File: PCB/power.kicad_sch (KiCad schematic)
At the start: 21 parts, among them U5 TLV62569DBVR, U6 TLV62569DBVR, U7 TLV62569DBVR

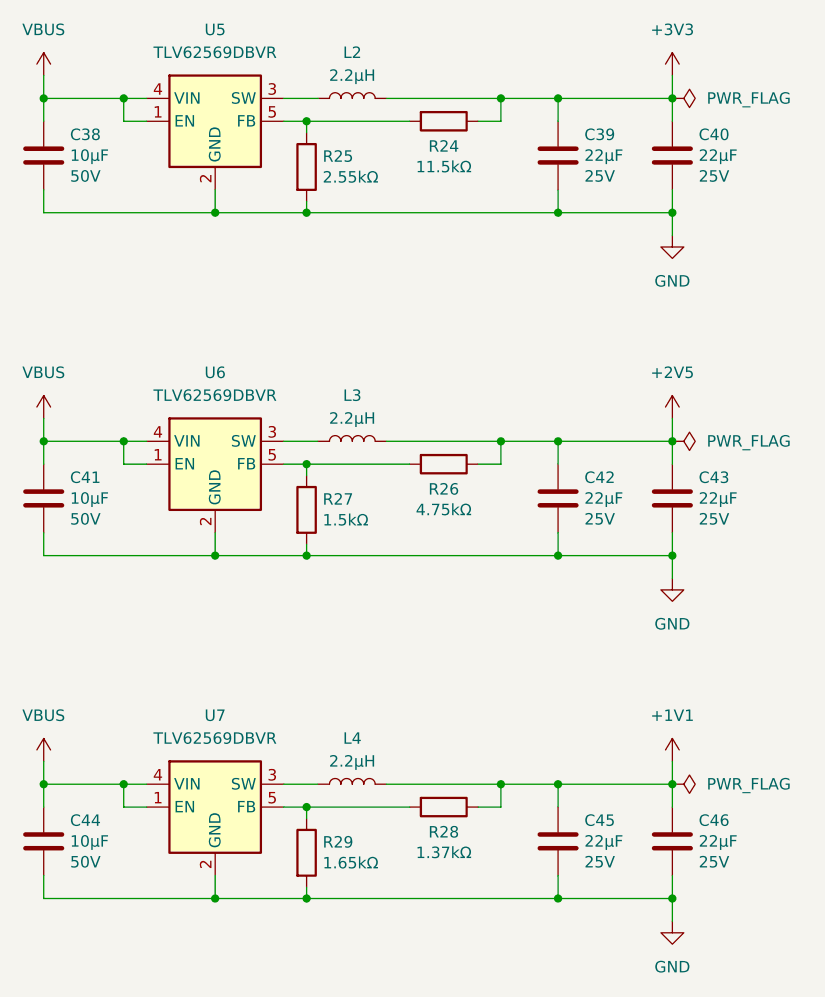
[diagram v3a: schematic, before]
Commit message: Improve the CH347F schematics and added 3D models
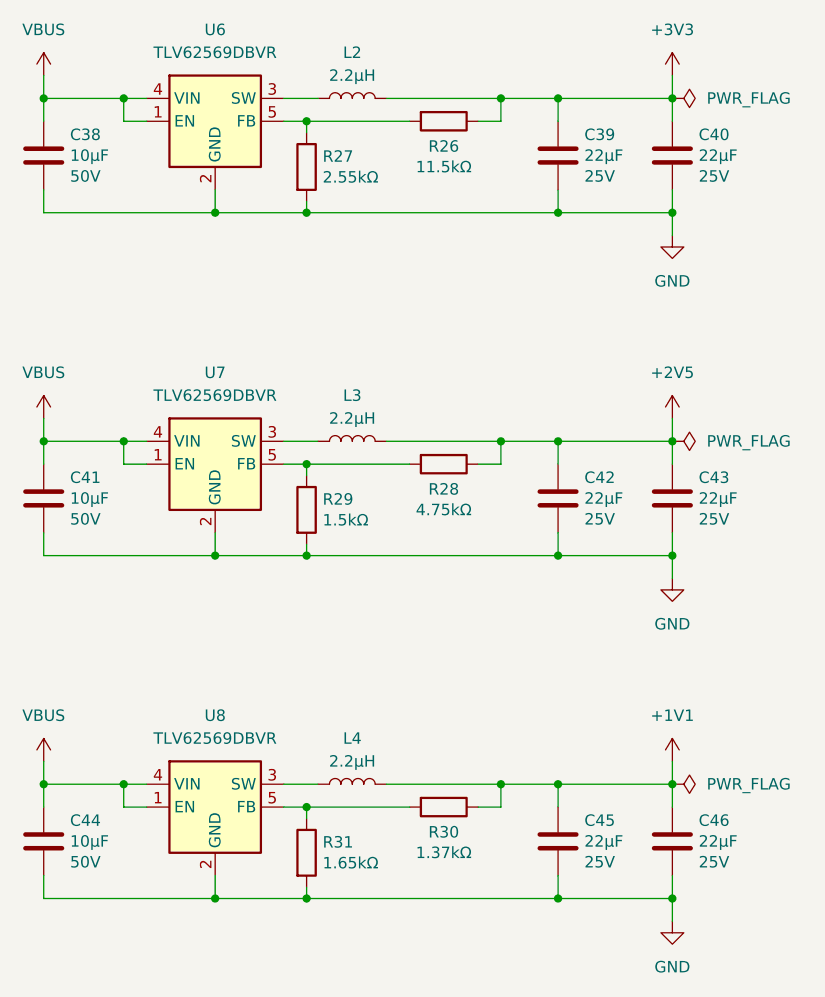
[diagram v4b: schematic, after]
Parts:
- renumbered R24 to R26, R25 to R27, R26 to R28, R27 to R29, R28 to R30, R29 to R31, U5 to U6, U6 to U7, U7 to U8
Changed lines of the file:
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@@
 		(dnp no)
 		(fields_autoplaced yes)
-		(property "Reference" "#PWR071"
+		(property "Reference" "#PWR075"
 			(at 171.45 110.49 0)
 			(effects
@@
 			(project "clavier"
 				(path "/6362c6e0-59ef-40d3-b6e0-7e9dfe7b9b20/0c8a9398-ddd2-4230-9850-fe0f46e922ad"
-					(reference "#PWR071")
+					(reference "#PWR075")
 					(unit 1)
 				)
@@
 		(dnp no)
 		(fields_autoplaced yes)
-		(property "Reference" "U5"
+		(property "Reference" "U6"
 			(at 120.65 43.18 0)
 			(effects
@@
 			(project ""
 				(path "/6362c6e0-59ef-40d3-b6e0-7e9dfe7b9b20/0c8a9398-ddd2-4230-9850-fe0f46e922ad"
-					(reference "U5")
+					(reference "U6")
 					(unit 1)
 				)
@@
 		(dnp no)
 		(fields_autoplaced yes)
-		(property "Reference" "#PWR068"
+		(property "Reference" "#PWR072"
 			(at 171.45 72.39 0)
 			(effects
@@
 			(project "clavier"
 				(path "/6362c6e0-59ef-40d3-b6e0-7e9dfe7b9b20/0c8a9398-ddd2-4230-9850-fe0f46e922ad"
-					(reference "#PWR068")
+					(reference "#PWR072")
 					(unit 1)
 				)
@@
 		(on_board yes)
 		(dnp no)
-		(property "Reference" "R24"
+		(property "Reference" "R26"
 			(at 146.05 56.134 90)
 			(effects
@@
 			(project "clavier"
 				(path "/6362c6e0-59ef-40d3-b6e0-7e9dfe7b9b20/0c8a9398-ddd2-4230-9850-fe0f46e922ad"
-					(reference "R24")
+					(reference "R26")
 					(unit 1)
 				)
@@
 		(dnp no)
 		(fields_autoplaced yes)
-		(property "Reference" "U6"
+		(property "Reference" "U7"
 			(at 120.65 81.28 0)
 			(effects
@@
 			(project "clavier"
 				(path "/6362c6e0-59ef-40d3-b6e0-7e9dfe7b9b20/0c8a9398-ddd2-4230-9850-fe0f46e922ad"
-					(reference "U6")
+					(reference "U7")
 					(unit 1)
 				)
@@
 		(dnp no)
 		(fields_autoplaced yes)
-		(property "Reference" "U7"
+		(property "Reference" "U8"
 			(at 120.65 119.38 0)
 			(effects
@@
 			(project "clavier"
 				(path "/6362c6e0-59ef-40d3-b6e0-7e9dfe7b9b20/0c8a9398-ddd2-4230-9850-fe0f46e922ad"
-					(reference "U7")
+					(reference "U8")
 					(unit 1)
 				)
@@
 		(dnp no)
 		(fields_autoplaced yes)
-		(property "Reference" "#PWR072"
+		(property "Reference" "#PWR076"
 			(at 101.6 128.27 0)
 			(effects
@@
 			(project "clavier"
 				(path "/6362c6e0-59ef-40d3-b6e0-7e9dfe7b9b20/0c8a9398-ddd2-4230-9850-fe0f46e922ad"
-					(reference "#PWR072")
+					(reference "#PWR076")
 					(unit 1)
 				)
@@
 		(dnp no)
 		(fields_autoplaced yes)
-		(property "Reference" "#PWR074"
+		(property "Reference" "#PWR078"
 			(at 171.45 148.59 0)
 			(effects
@@
 			(project "clavier"
 				(path "/6362c6e0-59ef-40d3-b6e0-7e9dfe7b9b20/0c8a9398-ddd2-4230-9850-fe0f46e922ad"
-					(reference "#PWR074")
+					(reference "#PWR078")
 					(unit 1)
 				)
@@
 		(dnp no)
 		(fields_autoplaced yes)
-		(property "Reference" "#PWR066"
+		(property "Reference" "#PWR070"
 			(at 101.6 52.07 0)
 			(effects
@@
 			(project ""
 				(path "/6362c6e0-59ef-40d3-b6e0-7e9dfe7b9b20/0c8a9398-ddd2-4230-9850-fe0f46e922ad"
-					(reference "#PWR066")
+					(reference "#PWR070")
 					(unit 1)
 				)
@@
 		(on_board yes)
 		(dnp no)
-		(property "Reference" "R26"
+		(property "Reference" "R28"
 			(at 146.05 94.234 90)
 			(effects
@@
 			(project "clavier"
 				(path "/6362c6e0-59ef-40d3-b6e0-7e9dfe7b9b20/0c8a9398-ddd2-4230-9850-fe0f46e922ad"
-					(reference "R26")
+					(reference "R28")
 					(unit 1)
 				)
@@
 		(on_board yes)
 		(dnp no)
-		(property "Reference" "R28"
+		(property "Reference" "R30"
 			(at 146.05 132.334 90)
 			(effects
@@
 			(project "clavier"
 				(path "/6362c6e0-59ef-40d3-b6e0-7e9dfe7b9b20/0c8a9398-ddd2-4230-9850-fe0f46e922ad"
-					(reference "R28")
+					(reference "R30")
 					(unit 1)
 				)
@@
 		(dnp no)
 		(fields_autoplaced yes)
-		(property "Reference" "#PWR069"
+		(property "Reference" "#PWR073"
 			(at 101.6 90.17 0)
 			(effects
@@
 			(project "clavier"
 				(path "/6362c6e0-59ef-40d3-b6e0-7e9dfe7b9b20/0c8a9398-ddd2-4230-9850-fe0f46e922ad"
-					(reference "#PWR069")
+					(reference "#PWR073")
 					(unit 1)
 				)
@@
 		(on_board yes)
 		(dnp no)
-		(property "Reference" "R27"
+		(property "Reference" "R29"
 			(at 132.588 95.3516 0)
 			(effects
@@
 			(project "clavier"
 				(path "/6362c6e0-59ef-40d3-b6e0-7e9dfe7b9b20/0c8a9398-ddd2-4230-9850-fe0f46e922ad"
-					(reference "R27")
+					(reference "R29")
 					(unit 1)
 				)
@@
 		(dnp no)
 		(fields_autoplaced yes)
-		(property "Reference" "#PWR067"
+		(property "Reference" "#PWR071"
 			(at 171.45 52.07 0)
 			(effects
@@
 			(project "clavier"
 				(path "/6362c6e0-59ef-40d3-b6e0-7e9dfe7b9b20/0c8a9398-ddd2-4230-9850-fe0f46e922ad"
-					(reference "#PWR067")
+					(reference "#PWR071")
 					(unit 1)
 				)
@@
 		(dnp no)
 		(fields_autoplaced yes)
-		(property "Reference" "#PWR073"
+		(property "Reference" "#PWR077"
 			(at 171.45 128.27 0)
 			(effects
@@
 			(project "clavier"
 				(path "/6362c6e0-59ef-40d3-b6e0-7e9dfe7b9b20/0c8a9398-ddd2-4230-9850-fe0f46e922ad"
-					(reference "#PWR073")
+					(reference "#PWR077")
 					(unit 1)
 				)
@@
 		(on_board yes)
 		(dnp no)
-		(property "Reference" "R29"
+		(property "Reference" "R31"
 			(at 132.588 133.4516 0)
 			(effects
@@
 			(project "clavier"
 				(path "/6362c6e0-59ef-40d3-b6e0-7e9dfe7b9b20/0c8a9398-ddd2-4230-9850-fe0f46e922ad"
-					(reference "R29")
+					(reference "R31")
 					(unit 1)
 				)
@@
 		(on_board yes)
 		(dnp no)
-		(property "Reference" "R25"
+		(property "Reference" "R27"
 			(at 132.588 57.2516 0)
 			(effects
@@
 			(project "clavier"
 				(path "/6362c6e0-59ef-40d3-b6e0-7e9dfe7b9b20/0c8a9398-ddd2-4230-9850-fe0f46e922ad"
-					(reference "R25")
+					(reference "R27")
 					(unit 1)
 				)
@@
 		(dnp no)
 		(fields_autoplaced yes)
-		(property "Reference" "#PWR070"
+		(property "Reference" "#PWR074"
 			(at 171.45 90.17 0)
 			(effects
@@
 			(project "clavier"
 				(path "/6362c6e0-59ef-40d3-b6e0-7e9dfe7b9b20/0c8a9398-ddd2-4230-9850-fe0f46e922ad"
-					(reference "#PWR070")
-					(unit 1)
-				)
+					(reference "#PWR074")
+					(unit 1)
+				)

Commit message: Add LICENSE and minor improvements
- Filled the title blocks
- Connected the LEDs to the FPGA
- Changed the FPGA programming header
- Added USB fuse and capacitors
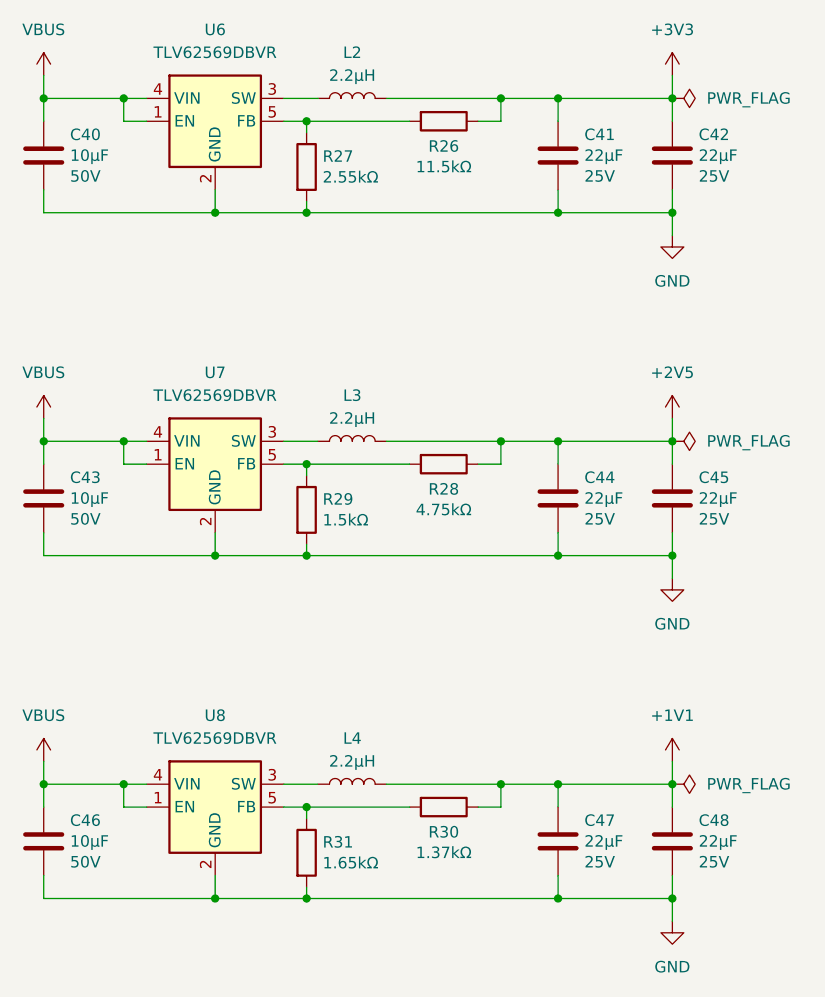
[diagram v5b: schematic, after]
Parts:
- renumbered C38 to C40, C39 to C41, C40 to C42, C41 to C43, C42 to C44, C43 to C45, C44 to C46, C45 to C47, C46 to C48
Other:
- company: (none) -> Copyright (c) 2025 L. Sartory
- title: (none) -> Clavier - Power supplies
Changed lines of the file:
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@@
 	(generator_version "9.0")
 	(paper "A4")
+	(title_block
+		(title "Clavier - Power supplies")
+		(date "2025-06-01")
+		(rev "1.0")
+		(company "Copyright (c) 2025 L. Sartory")
+		(comment 1 "SPDX-License-Identifier: CERN-OHL-P-2.0")
+	)
 	(junction
 		(at 120.65 101.6)
@@
 		(dnp no)
 		(fields_autoplaced yes)
-		(property "Reference" "#PWR075"
+		(property "Reference" "#PWR074"
 			(at 171.45 110.49 0)
 			(effects
@@
 			(project "clavier"
 				(path "/6362c6e0-59ef-40d3-b6e0-7e9dfe7b9b20/0c8a9398-ddd2-4230-9850-fe0f46e922ad"
-					(reference "#PWR075")
+					(reference "#PWR074")
 					(unit 1)
 				)
@@
 		(dnp no)
 		(fields_autoplaced yes)
-		(property "Reference" "#PWR072"
+		(property "Reference" "#PWR071"
 			(at 171.45 72.39 0)
 			(effects
@@
 			(project "clavier"
 				(path "/6362c6e0-59ef-40d3-b6e0-7e9dfe7b9b20/0c8a9398-ddd2-4230-9850-fe0f46e922ad"
-					(reference "#PWR072")
+					(reference "#PWR071")
 					(unit 1)
 				)
@@
 		(on_board yes)
 		(dnp no)
-		(property "Reference" "C40"
+		(property "Reference" "C42"
 			(at 174.371 54.8386 0)
 			(effects
@@
 			(project "clavier"
 				(path "/6362c6e0-59ef-40d3-b6e0-7e9dfe7b9b20/0c8a9398-ddd2-4230-9850-fe0f46e922ad"
-					(reference "C40")
+					(reference "C42")
 					(unit 1)
 				)
@@
 		(on_board yes)
 		(dnp no)
-		(property "Reference" "C42"
+		(property "Reference" "C44"
 			(at 161.671 92.9386 0)
 			(effects
@@
 			(project "clavier"
 				(path "/6362c6e0-59ef-40d3-b6e0-7e9dfe7b9b20/0c8a9398-ddd2-4230-9850-fe0f46e922ad"
-					(reference "C42")
+					(reference "C44")
 					(unit 1)
 				)
@@
 		(dnp no)
 		(fields_autoplaced yes)
-		(property "Reference" "#PWR076"
+		(property "Reference" "#PWR075"
 			(at 101.6 128.27 0)
 			(effects
@@
 			(project "clavier"
 				(path "/6362c6e0-59ef-40d3-b6e0-7e9dfe7b9b20/0c8a9398-ddd2-4230-9850-fe0f46e922ad"
-					(reference "#PWR076")
+					(reference "#PWR075")
 					(unit 1)
 				)
@@
 		(on_board yes)
 		(dnp no)
-		(property "Reference" "C38"
+		(property "Reference" "C40"
 			(at 104.521 54.8386 0)
 			(effects
@@
 			(project "clavier"
 				(path "/6362c6e0-59ef-40d3-b6e0-7e9dfe7b9b20/0c8a9398-ddd2-4230-9850-fe0f46e922ad"
-					(reference "C38")
+					(reference "C40")
 					(unit 1)
 				)
@@
 		(dnp no)
 		(fields_autoplaced yes)
-		(property "Reference" "#PWR078"
+		(property "Reference" "#PWR077"
 			(at 171.45 148.59 0)
 			(effects
@@
 			(project "clavier"
 				(path "/6362c6e0-59ef-40d3-b6e0-7e9dfe7b9b20/0c8a9398-ddd2-4230-9850-fe0f46e922ad"
-					(reference "#PWR078")
+					(reference "#PWR077")
 					(unit 1)
 				)
@@
 		(dnp no)
 		(fields_autoplaced yes)
-		(property "Reference" "#PWR070"
+		(property "Reference" "#PWR069"
 			(at 101.6 52.07 0)
 			(effects
@@
 			(project ""
 				(path "/6362c6e0-59ef-40d3-b6e0-7e9dfe7b9b20/0c8a9398-ddd2-4230-9850-fe0f46e922ad"
-					(reference "#PWR070")
+					(reference "#PWR069")
 					(unit 1)
 				)
@@
 		(dnp no)
 		(fields_autoplaced yes)
-		(property "Reference" "#PWR073"
+		(property "Reference" "#PWR072"
 			(at 101.6 90.17 0)
 			(effects
@@
 			(project "clavier"
 				(path "/6362c6e0-59ef-40d3-b6e0-7e9dfe7b9b20/0c8a9398-ddd2-4230-9850-fe0f46e922ad"
-					(reference "#PWR073")
+					(reference "#PWR072")
 					(unit 1)
 				)
@@
 		(on_board yes)
 		(dnp no)
-		(property "Reference" "C46"
+		(property "Reference" "C48"
 			(at 174.371 131.0386 0)
 			(effects
@@
 			(project "clavier"
 				(path "/6362c6e0-59ef-40d3-b6e0-7e9dfe7b9b20/0c8a9398-ddd2-4230-9850-fe0f46e922ad"
-					(reference "C46")
+					(reference "C48")
 					(unit 1)
 				)
@@
 		(dnp no)
 		(fields_autoplaced yes)
-		(property "Reference" "#PWR071"
+		(property "Reference" "#PWR070"
 			(at 171.45 52.07 0)
 			(effects
@@
 			(project "clavier"
 				(path "/6362c6e0-59ef-40d3-b6e0-7e9dfe7b9b20/0c8a9398-ddd2-4230-9850-fe0f46e922ad"
-					(reference "#PWR071")
+					(reference "#PWR070")
 					(unit 1)
 				)
@@
 		(on_board yes)
 		(dnp no)
-		(property "Reference" "C45"
+		(property "Reference" "C47"
 			(at 161.671 131.0386 0)
 			(effects
@@
 			(project "clavier"
 				(path "/6362c6e0-59ef-40d3-b6e0-7e9dfe7b9b20/0c8a9398-ddd2-4230-9850-fe0f46e922ad"
-					(reference "C45")
+					(reference "C47")
 					(unit 1)
 				)
@@
 		(dnp no)
 		(fields_autoplaced yes)
-		(property "Reference" "#PWR077"
+		(property "Reference" "#PWR076"
 			(at 171.45 128.27 0)
 			(effects
@@
 			(project "clavier"
 				(path "/6362c6e0-59ef-40d3-b6e0-7e9dfe7b9b20/0c8a9398-ddd2-4230-9850-fe0f46e922ad"
-					(reference "#PWR077")
+					(reference "#PWR076")
 					(unit 1)
 				)
@@
 		(on_board yes)
 		(dnp no)
-		(property "Reference" "C39"
+		(property "Reference" "C41"
 			(at 161.671 54.8386 0)
 			(effects
@@
 			(project "clavier"
 				(path "/6362c6e0-59ef-40d3-b6e0-7e9dfe7b9b20/0c8a9398-ddd2-4230-9850-fe0f46e922ad"
-					(reference "C39")
+					(reference "C41")
 					(unit 1)
 				)
@@
 		(on_board yes)
 		(dnp no)
-		(property "Reference" "C44"
+		(property "Reference" "C46"
 			(at 104.521 131.0386 0)
 			(effects
@@
 			(project "clavier"
 				(path "/6362c6e0-59ef-40d3-b6e0-7e9dfe7b9b20/0c8a9398-ddd2-4230-9850-fe0f46e922ad"
-					(reference "C44")
+					(reference "C46")
 					(unit 1)
 				)
@@
 		(on_board yes)
 		(dnp no)
-		(property "Reference" "C41"
+		(property "Reference" "C43"
 			(at 104.521 92.9386 0)
 			(effects
@@
 			(project "clavier"
 				(path "/6362c6e0-59ef-40d3-b6e0-7e9dfe7b9b20/0c8a9398-ddd2-4230-9850-fe0f46e922ad"
-					(reference "C41")
+					(reference "C43")
 					(unit 1)
 				)
@@
 		(dnp no)
 		(fields_autoplaced yes)
-		(property "Reference" "#PWR074"
+		(property "Reference" "#PWR073"
 			(at 171.45 90.17 0)
 			(effects
@@
 			(project "clavier"
 				(path "/6362c6e0-59ef-40d3-b6e0-7e9dfe7b9b20/0c8a9398-ddd2-4230-9850-fe0f46e922ad"
-					(reference "#PWR074")
+					(reference "#PWR073")
 					(unit 1)
 				)
@@
 		(on_board yes)
 		(dnp no)
-		(property "Reference" "C43"
+		(property "Reference" "C45"
 			(at 174.371 92.9386 0)
 			(effects
@@
 			(project "clavier"
 				(path "/6362c6e0-59ef-40d3-b6e0-7e9dfe7b9b20/0c8a9398-ddd2-4230-9850-fe0f46e922ad"
-					(reference "C43")
+					(reference "C45")
 					(unit 1)
 				)
